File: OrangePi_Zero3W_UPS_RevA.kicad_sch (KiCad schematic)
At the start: 0 parts

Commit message: update phase 5A.1
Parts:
- added J1: ORANGE_PI_ZERO_3W_HEADER, Connector_PinSocket_2.54mm:PinSocket_2x20_P2.54mm_Vertical, symbol Connector_Generic:Conn_02x20_Odd_Even
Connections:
- new net GND: J1.10 (Pin_10), J1.13 (Pin_13), J1.19 (Pin_19), J1.26 (Pin_26), J1.29 (Pin_29), J1.33 (Pin_33), J1.40 (Pin_40), J1.5 (Pin_5)
- new net HOST_3V3: J1.2 (Pin_2)
- new net I2C_SCL: J1.6 (Pin_6)
- new net I2C_SDA: J1.4 (Pin_4)
- new net UPS_5V: J1.1 (Pin_1), J1.3 (Pin_3)
- no-connect marks 0 -> 27

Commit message: phase 5A.2
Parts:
- added C1: 100nF, Capacitor_SMD:C_0603_1608Metric, symbol Device:C
- added R1, R2: 4.7k, Resistor_SMD:R_0603_1608Metric, symbol Device:R
- added U1: MAX17048G_T10, MAX17048G_T10:SON50P200X200X80-9N, symbol MAX17048G_T10:MAX17048G_T10
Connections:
- net GND: now also C1.2, U1.1 (CTG), U1.4 (GND), U1.6 (QSTRT), U1.9 (EP)
- net HOST_3V3: now also R1.1, R2.1
- net I2C_SCL: now also R2.2, U1.7 (SCL)
- net I2C_SDA: now also R1.2, U1.8 (SDA)
- new net BAT_POS: C1.1, U1.2 (CELL), U1.3 (VDD)
- no-connect marks 27 -> 28
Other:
- note added: "MAX17048G+T10 1-cell Li-ion fuel gauge I2C 7-bit address: 0x36 ALRT unused in Rev A"

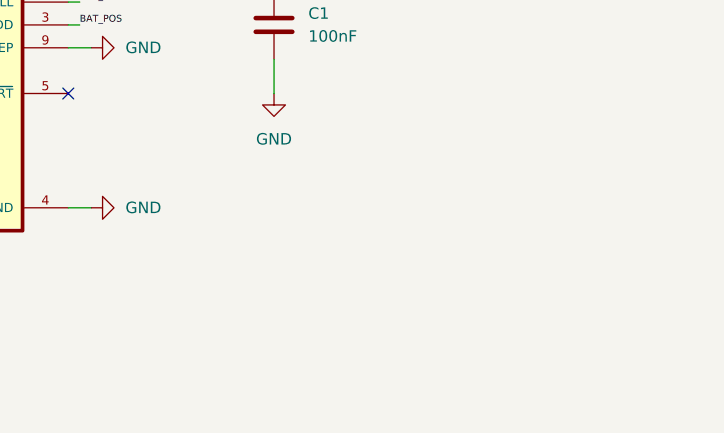
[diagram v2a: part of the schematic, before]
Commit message: Phase 5A.3: add provisional protected battery interface
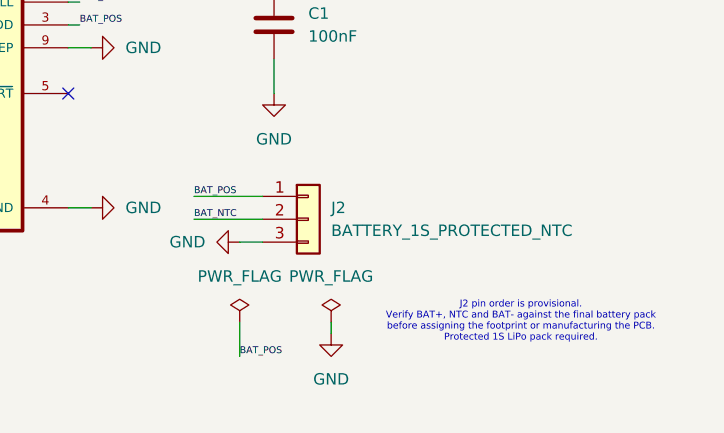
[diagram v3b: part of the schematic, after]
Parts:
- added J2: BATTERY_1S_PROTECTED_NTC, symbol Connector_Generic:Conn_01x03
- U1: Description_1 3µA 1-Cell/2-Cell Fuel Gauge with ModelGauge -> 1-Cell Li-ion Fuel Gauge with ModelGauge; MP MAX17048G+T10 -> (none); MPN (none) -> MAX17048G+T10; Package TDFN-8 Maxim -> TDFN-8-EP, T822+3
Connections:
- net BAT_POS: now also J2.1 (Pin_1)
- net GND: now also J2.3 (Pin_3)
- new net BAT_NTC: J2.2 (Pin_2)
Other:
- note added: "J2 pin order is provisional. Verify BAT+, NTC and BAT- against the final battery pack before assigning the footprint or manufacturing the PCB. Protected 1S LiPo pack required."

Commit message: phase 5B.1B
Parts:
- added C2, C3, C4: 10uF, Capacitor_SMD:C_0805_2012Metric, symbol Device:C
- added R3, R4: 10k, Resistor_SMD:R_0603_1608Metric, symbol Device:R
- added SW1: POWER / QON, symbol Switch:SW_Push
- added U2: BQ25895RTWR, BQ25895RTWR:QFN50P400X400X80-25N, symbol BQ25895RTWR:BQ25895RTWR
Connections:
- net GND: now also C2.2, C3.2, C4.2, R3.2, R4.2, SW1.1, U2.17 (PGND), U2.18 (PGND), U2.25 (POWERPAD)
- net BAT_POS renamed BAT
- net BAT: now also C2.1, U2.13 (BAT), U2.14 (BAT)
- new net: SW1.2, U2.12 (~{QON})
- new net: R4.1, U2.8 (OTG)
- new net: R3.1, U2.9 (~{CE})
- new net SW: U2.19 (SW), U2.20 (SW)
- new net SYS: C3.1, C4.1, U2.15 (SYS), U2.16 (SYS)
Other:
- note added: "BQ25895RTWR 1-cell charger + NVDC power path I2C 7-bit address: 0x6A"
- moved on the sheet: C1, J1, J2, R1, R2, U1

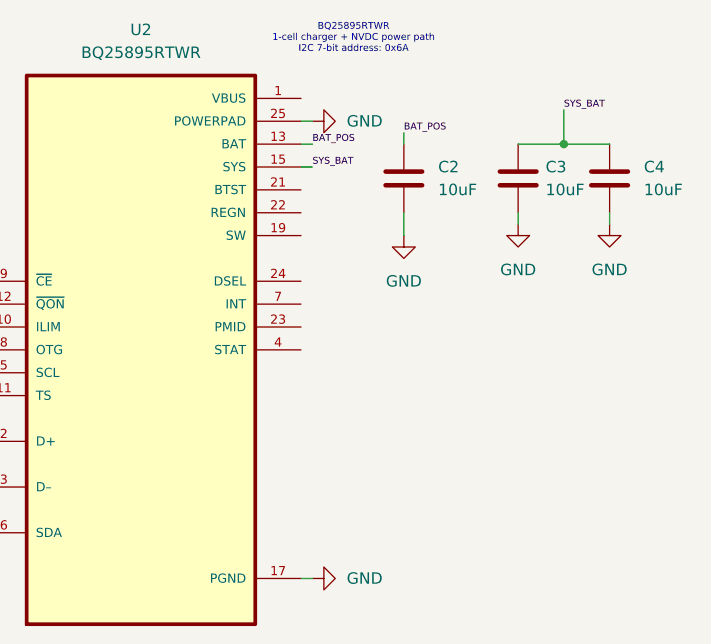
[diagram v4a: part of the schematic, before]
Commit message: Phase 5B.1C: add BQ25895 switching and bias components
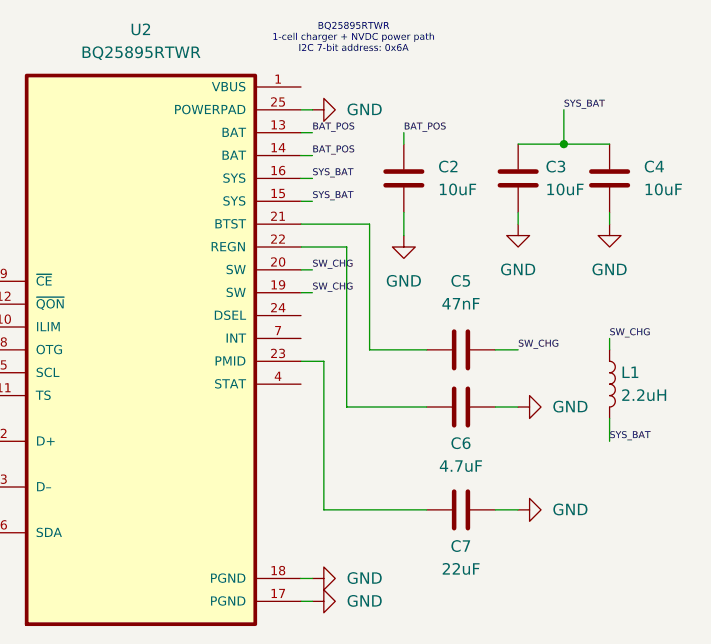
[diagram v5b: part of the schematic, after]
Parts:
- added C5: 47nF, Capacitor_SMD:C_0402_1005Metric, symbol Device:C
- added C6: 4.7uF, Capacitor_SMD:C_0603_1608Metric, symbol Device:C
- added C7: 22uF, Capacitor_SMD:C_0805_2012Metric, symbol Device:C
- added L1: 2.2uH, symbol Device:L
- U2: MP (none) -> BQ25895RTWR; Package WQFN-24-EP, RTW, 4x4 mm -> WQFN-24 Texas Instruments
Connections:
- net GND: now also C6.1, C7.2
- net at U2.21 (BTST): now also C5.2
- net at U2.22 (REGN): now also C6.2
- net at U2.23 (PMID): now also C7.1
- net BAT renamed BAT_POS
- net SW renamed SW_CHG
- net SW_CHG: now also C5.1, L1.1
- net SYS renamed SYS_BAT
- net SYS_BAT: now also L1.2

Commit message: Phase 5B.1D: add charger I2C, ILIM and battery temperature network
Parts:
- added R5: 130, Resistor_SMD:R_0603_1608Metric, symbol Device:R
- added R6: 5.23k, Resistor_SMD:R_0603_1608Metric, symbol Device:R
- added R7: 30.1k, Resistor_SMD:R_0603_1608Metric, symbol Device:R
- added R8: 10k, Resistor_SMD:R_0603_1608Metric, symbol Device:R
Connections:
- net BAT_NTC: now also U2.11 (TS), R6.1, R7.2
- net GND: now also R5.1, R7.1
- net HOST_3V3: now also R8.1
- net I2C_SCL: now also U2.5 (SCL)
- net I2C_SDA: now also U2.6 (SDA)
- net at U2.10 (ILIM): now also R5.2
- net at U2.24 (DSEL): now also R8.2
- new net REGN: R6.2
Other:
- moved on the sheet: L1

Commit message: Phase 5B.1E: finalize BQ25895 control and status pins
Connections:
- net REGN: now also C6.2, U2.22 (REGN)
- no-connect marks 28 -> 30
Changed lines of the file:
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@@
+	)
+	(no_connect
+		(at 238.76 49.53)
 	)
 	(no_connect
@@
 	(no_connect
 		(at 21.59 54.61)
+	)
+	(no_connect
+		(at 238.76 54.61)
 	)
 	(no_connect
@@
 		(effects
 			(font
+				(size 0.762 0.762)
+			)
+			(justify left bottom)
+		)
+	)
+	(label "REGN"
+		(at 243.84 55.88 0)
+		(effects
+			(font
